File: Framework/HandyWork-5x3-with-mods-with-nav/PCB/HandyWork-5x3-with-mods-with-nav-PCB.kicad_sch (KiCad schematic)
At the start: 52 parts, among them J1 Conn_01x04, J2 Conn_02x04_Odd_Even, SW1 KXT3, SW2 KXT3, U1 RP2040, U2 W25Q16JV, U3 IS31FL3733B-QF, Y1 12.000 MHz

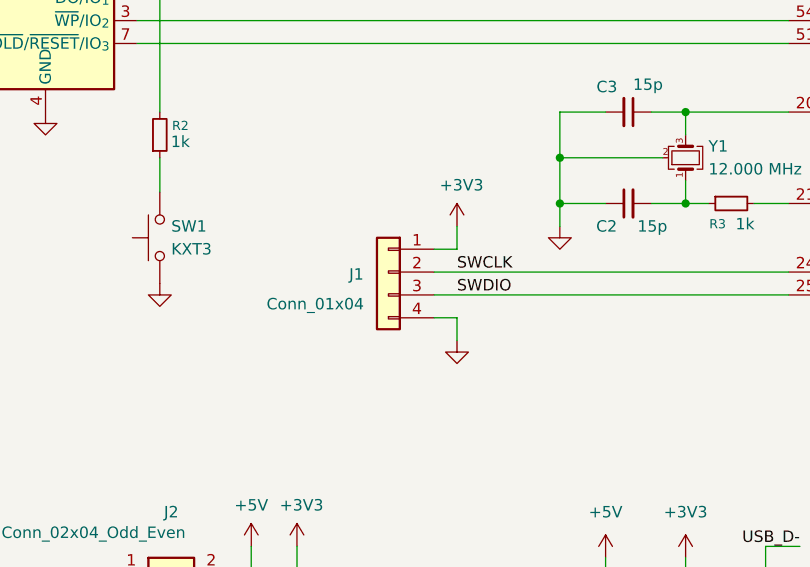
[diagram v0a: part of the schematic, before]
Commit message: HandyWork 5x3 + Mods + Nav: Adjustements for fabrication outputs
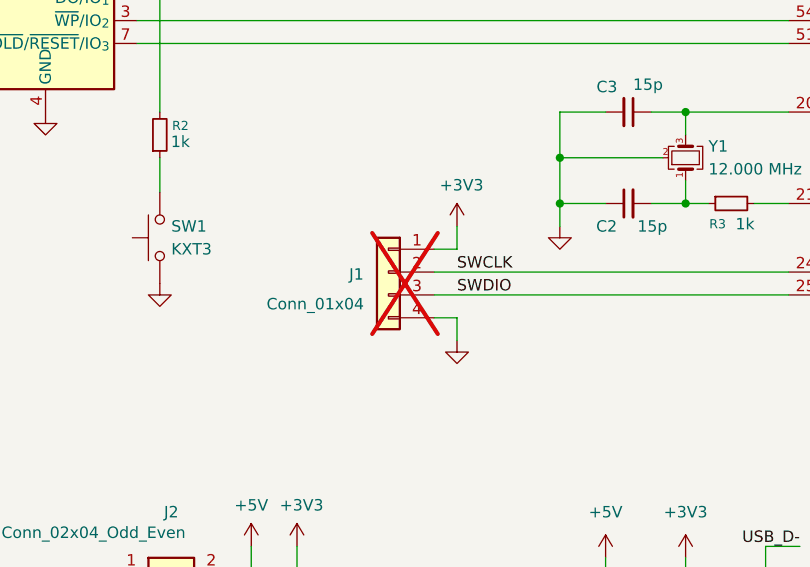
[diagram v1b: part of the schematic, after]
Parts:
- J1: now not fitted
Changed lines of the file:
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@@
 		(in_bom no)
 		(on_board yes)
-		(dnp no)
+		(dnp yes)
 		(property "Reference" "J1"
 			(at 65.024 134.874 0)

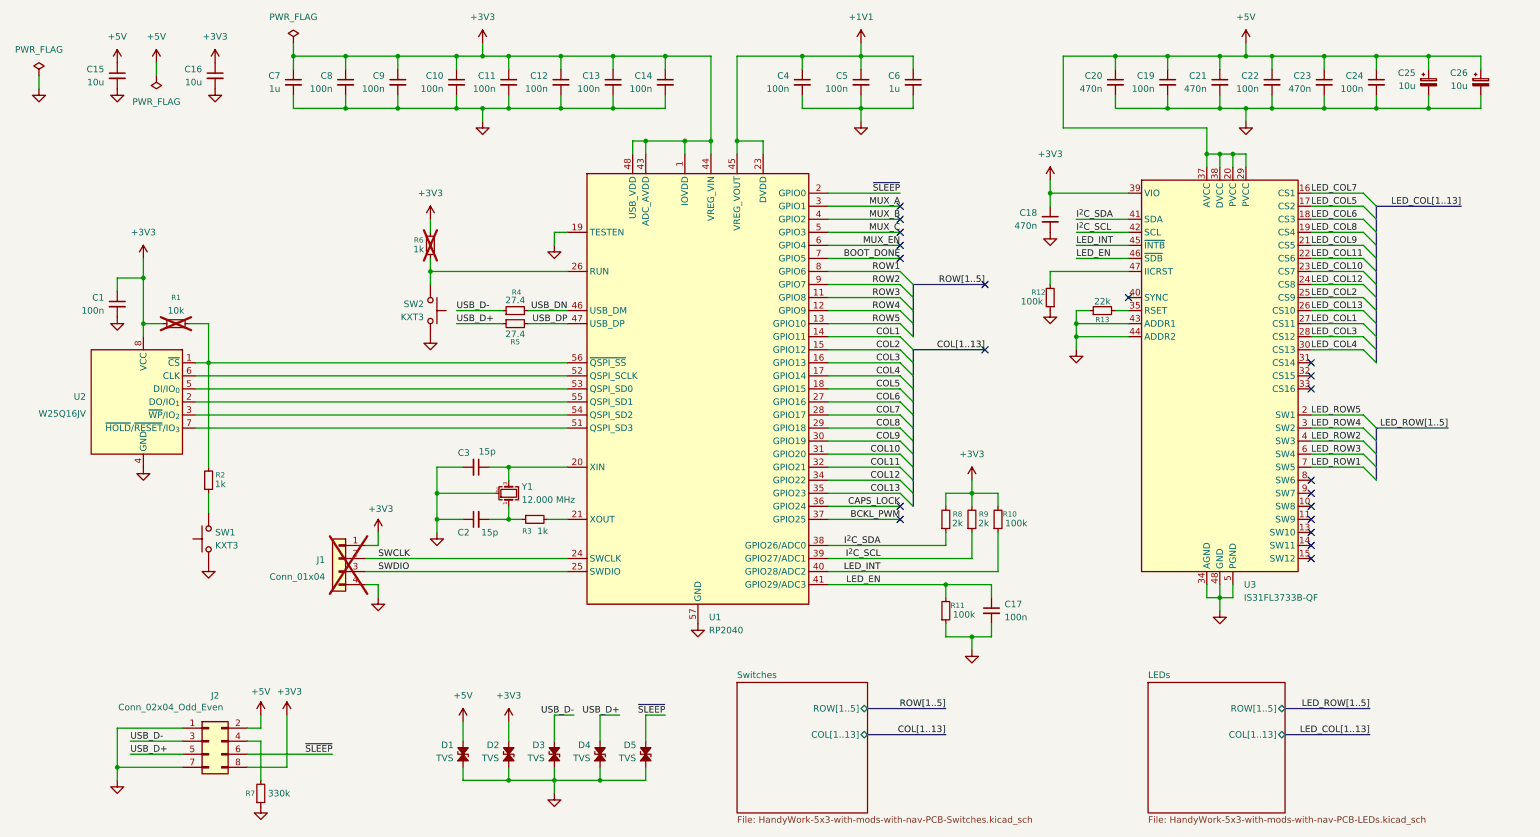
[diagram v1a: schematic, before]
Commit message: HandyWork: Refactor vias to not use 0.2mm drill in order to be significantly cheaper (~50% for the PCB itself)
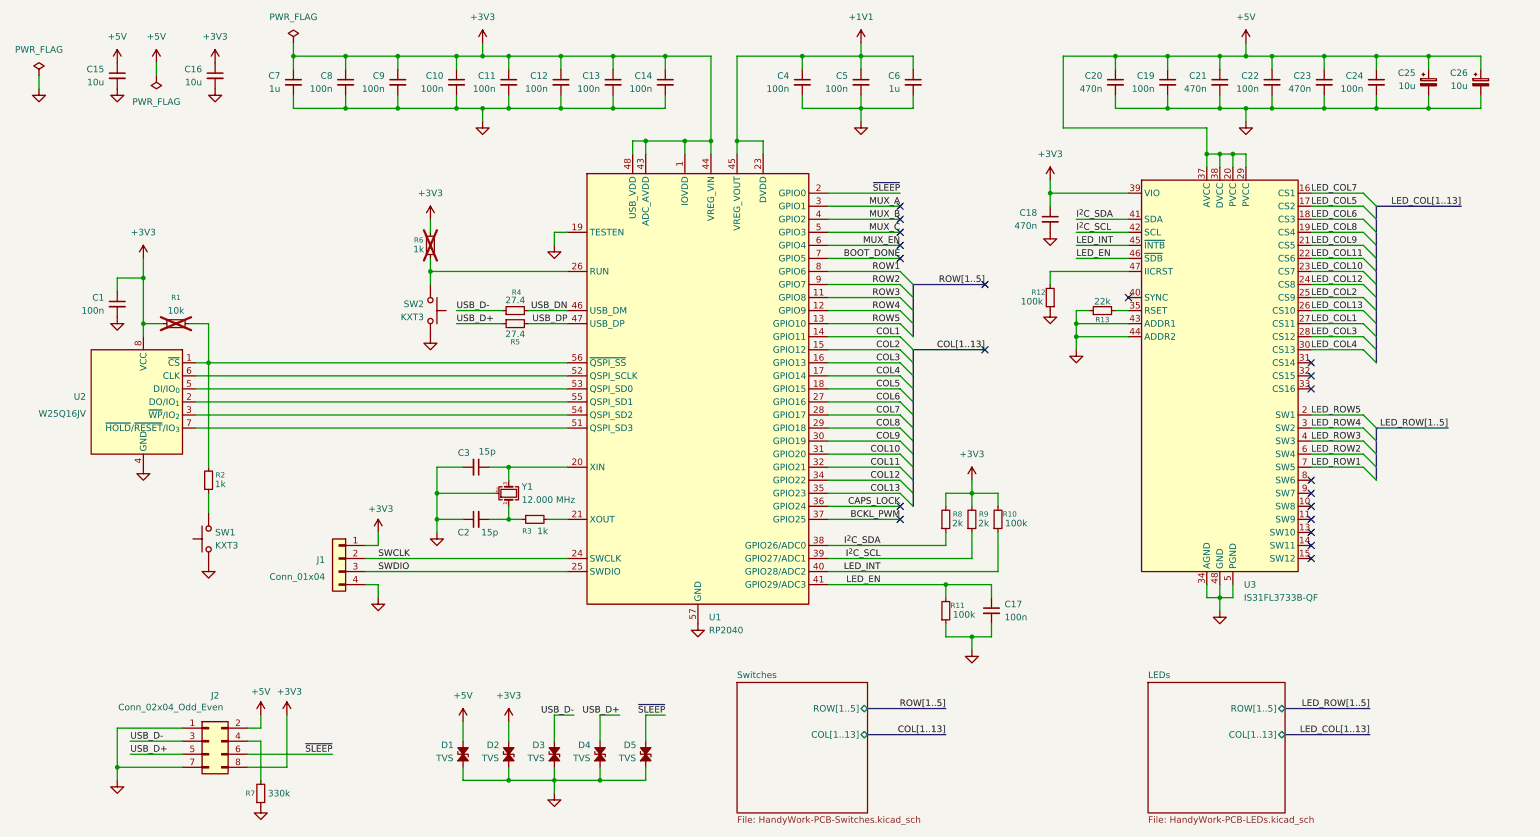
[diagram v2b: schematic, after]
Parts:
- J1: now fitted
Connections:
- net LED_ROW2: now also U3.6 (SW4); no longer U3.4 (SW3)
- net LED_ROW3: now also U3.4 (SW3); no longer U3.6 (SW4)
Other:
- sheet LEDs: file HandyWork-5x3-with-mods-with-nav-PCB-LEDs.kicad_sch -> HandyWork-PCB-LEDs.kicad_sch
- sheet Switches: file HandyWork-5x3-with-mods-with-nav-PCB-Switches.kicad_sch -> HandyWork-PCB-Switches.kicad_sch
- title: HandyWork - 5x3 + Mods + Nav -> HandyWork - PCB Template

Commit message: HandyWork 5x3-M-N: Fixing the schematic that got broken by raw copying it from the template
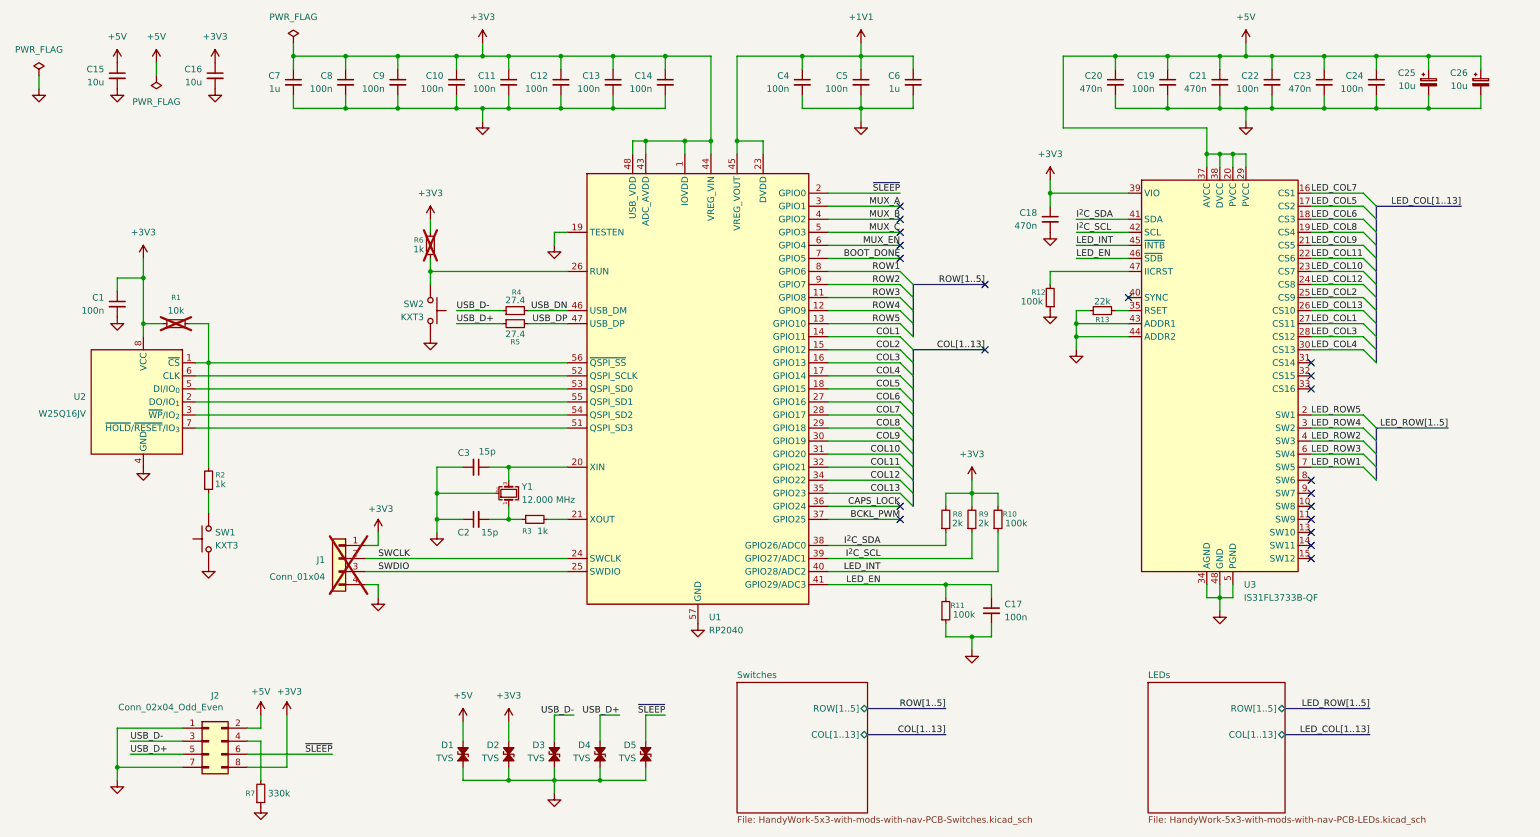
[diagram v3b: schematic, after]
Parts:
- J1: now not fitted
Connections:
- net LED_ROW2: now also U3.4 (SW3); no longer U3.6 (SW4)
- net LED_ROW3: now also U3.6 (SW4); no longer U3.4 (SW3)
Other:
- sheet LEDs: file HandyWork-PCB-LEDs.kicad_sch -> HandyWork-5x3-with-mods-with-nav-PCB-LEDs.kicad_sch
- sheet Switches: file HandyWork-PCB-Switches.kicad_sch -> HandyWork-5x3-with-mods-with-nav-PCB-Switches.kicad_sch
- title: HandyWork - PCB Template -> HandyWork - 5x3 + Mods + Nav

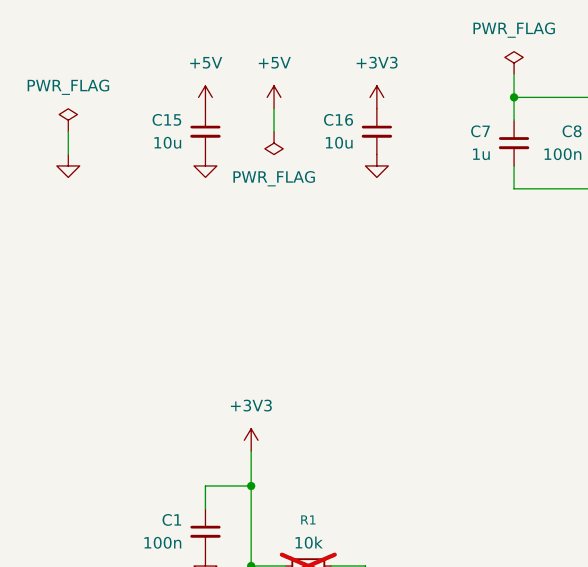
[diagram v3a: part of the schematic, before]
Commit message: HandyWork: Harmonise a few things, and add bind points with alu plates
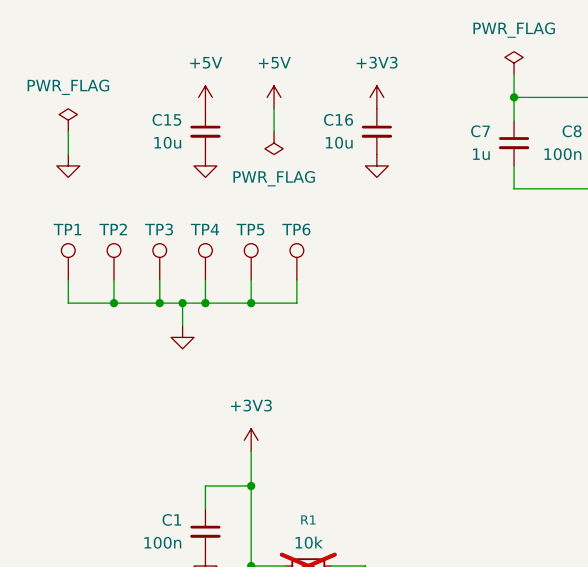
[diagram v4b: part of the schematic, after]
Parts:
- added TP1, TP2, TP3, TP4, TP5, TP6: TestPoint, TestPoint:TestPoint_THTPad_2.5x2.5mm_Drill1.2mm, symbol Connector:TestPoint
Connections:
- net GND: now also TP1.1, TP2.1, TP3.1, TP4.1, TP5.1, TP6.1
